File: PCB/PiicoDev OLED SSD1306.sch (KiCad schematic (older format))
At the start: 30 parts, among them J1 , J2 , J3 Conn_PiicoDev_header_01x04_Ma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, J4 Conn_01x01_Male, U2 Display_Graphic_OLED_SSD1306_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

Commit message: Update Schematic & PCB
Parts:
- added JP3: SolderJumper_2_Open, Jumper:SolderJumper-2_P1.3mm_Open_RoundedPad1.0x1.5mm, symbol Jumper:SolderJumper_2_Open
- added R6: 4k7, Resistor_SMD:R_0402_1005Metric, symbol Device:R
- C1: value 1.0u -> 2.2u; footprint Capacitor_SMD:C_0603_1608Metric -> Capacitor_SMD:C_0402_1005Metric
- C2, C3, C6, C7: footprint Capacitor_SMD:C_0603_1608Metric -> Capacitor_SMD:C_0402_1005Metric
- C4: value 100n -> 2.2u; footprint Capacitor_SMD:C_0603_1608Metric -> Capacitor_SMD:C_0402_1005Metric
- C5: value 10u -> 2.2u; footprint Capacitor_SMD:C_0603_1608Metric -> Capacitor_SMD:C_0402_1005Metric
- R1: value 1k -> 4k7
- R5: value 1K -> 4k7
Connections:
- net +3V3: now also JP3.1 (A)
- net GND: now also R6.2
- net SA0: now also JP3.2 (B), R6.1
- no-connect marks 6 -> 5
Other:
- note removed: "ToDo, check capacitor values against other designs"
- moved on the sheet: R4
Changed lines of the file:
@@
 encoding utf-8
 Sheet 1 1
-Title ""
-Date ""
-Rev ""
+Title "PiicoDev OLED SSD1306"
+Date "2021-07-09"
+Rev "00"
 Comp "Core Electronics"
-Comment1 ""
-Comment2 ""
-Comment3 ""
+Comment1 "Designed at Core Electronics by Peter Johnston"
+Comment2 "PiicoDev and the PiicoDev logo are trademarks of Core Electronics Pty Ltd"
+Comment3 "License: CCASAv4.0 http://creativecommons.org/licenses/by-sa/4.0"
 Comment4 ""
 $EndDescr
@@
 P 1450 3950
 F 0 "R1" H 1520 3996 50  0000 L CNN
-F 1 "1k" H 1520 3905 50  0000 L CNN
+F 1 "4k7" H 1520 3905 50  0000 L CNN
 F 2 "Resistor_SMD:R_0402_1005Metric" V 1380 3950 50  0001 C CNN
 F 3 "~" H 1450 3950 50  0001 C CNN
@@
 P 5400 5150
 F 0 "C1" H 5515 5196 50  0000 L CNN
-F 1 "1.0u" H 5515 5105 50  0000 L CNN
-F 2 "Capacitor_SMD:C_0603_1608Metric" H 5438 5000 50  0001 C CNN
+F 1 "2.2u" H 5515 5105 50  0000 L CNN
+F 2 "Capacitor_SMD:C_0402_1005Metric" H 5438 5000 50  0001 C CNN
 F 3 "~" H 5400 5150 50  0001 C CNN
 	1    5400 5150
@@
 F 0 "C2" H 9815 2096 50  0000 L CNN
 F 1 "2.2u" H 9815 2005 50  0000 L CNN
-F 2 "Capacitor_SMD:C_0603_1608Metric" H 9738 1900 50  0001 C CNN
+F 2 "Capacitor_SMD:C_0402_1005Metric" H 9738 1900 50  0001 C CNN
 F 3 "~" H 9700 2050 50  0001 C CNN
 	1    9700 2050
-	1    0    0    -1
-$EndComp
-$Comp
-L Device:C C4
-U 1 1 60E2EDE0
-P 5850 5150
-F 0 "C4" H 5965 5196 50  0000 L CNN
-F 1 "100n" H 5965 5105 50  0000 L CNN
-F 2 "Capacitor_SMD:C_0603_1608Metric" H 5888 5000 50  0001 C CNN
-F 3 "~" H 5850 5150 50  0001 C CNN
-	1    5850 5150
 	1    0    0    -1
 $EndComp
@@
 F 0 "C6" H 9365 2546 50  0000 L CNN
 F 1 "2.2u" H 9365 2455 50  0000 L CNN
-F 2 "Capacitor_SMD:C_0603_1608Metric" H 9288 2350 50  0001 C CNN
+F 2 "Capacitor_SMD:C_0402_1005Metric" H 9288 2350 50  0001 C CNN
 F 3 "~" H 9250 2500 50  0001 C CNN
 	1    9250 2500
@@
 L Device:R R4
 U 1 1 60E30177
-P 7500 3700
-F 0 "R4" H 7570 3746 50  0000 L CNN
-F 1 "390K" H 7570 3655 50  0000 L CNN
-F 2 "Resistor_SMD:R_0402_1005Metric" V 7430 3700 50  0001 C CNN
-F 3 "~" H 7500 3700 50  0001 C CNN
-	1    7500 3700
+P 7400 3700
+F 0 "R4" H 7470 3746 50  0000 L CNN
+F 1 "390K" H 7470 3655 50  0000 L CNN
+F 2 "Resistor_SMD:R_0402_1005Metric" V 7330 3700 50  0001 C CNN
+F 3 "~" H 7400 3700 50  0001 C CNN
+	1    7400 3700
 	1    0    0    -1
 $EndComp
@@
 F 0 "C3" H 9365 3746 50  0000 L CNN
 F 1 "2.2u" H 9365 3655 50  0000 L CNN
-F 2 "Capacitor_SMD:C_0603_1608Metric" H 9288 3550 50  0001 C CNN
+F 2 "Capacitor_SMD:C_0402_1005Metric" H 9288 3550 50  0001 C CNN
 F 3 "~" H 9250 3700 50  0001 C CNN
 	1    9250 3700
@@
 F 0 "C7" H 9365 3146 50  0000 L CNN
 F 1 "2.2u" H 9365 3055 50  0000 L CNN
-F 2 "Capacitor_SMD:C_0603_1608Metric" H 9288 2950 50  0001 C CNN
+F 2 "Capacitor_SMD:C_0402_1005Metric" H 9288 2950 50  0001 C CNN
 F 3 "~" H 9250 3100 50  0001 C CNN
 	1    9250 3100
@@
 $EndComp
 Wire Wire Line
-	6300 2600 6300 2700
-Wire Wire Line
 	6300 3500 6300 3600
 $Comp
@@
 	1    0    0    -1
 $EndComp
-Wire Wire Line
-	7950 3200 7700 3200
 Text Label 7700 3200 0    50   ~ 0
 SA0
@@
 Wire Wire Line
 	2950 2000 3150 2000
-Wire Wire Line
-	7500 5150 8400 5150
 Connection ~ 8400 5150
-Wire Wire Line
-	7500 3850 7500 5150
-Wire Wire Line
-	7400 3400 7400 5150
-Wire Wire Line
-	7400 5150 7500 5150
-Wire Wire Line
-	7400 3400 7950 3400
-Connection ~ 7500 5150
-Wire Wire Line
-	7400 3300 7400 3400
-Wire Wire Line
-	7400 3300 7950 3300
-Connection ~ 7400 3400
-Wire Wire Line
-	7950 3500 7500 3500
-Wire Wire Line
-	7500 3500 7500 3550
-Wire Wire Line
-	5400 5000 5400 4950
-Wire Wire Line
-	5400 4950 5850 4950
-Wire Wire Line
-	5850 4950 5850 5000
-Wire Wire Line
-	5400 5300 5400 5350
-Wire Wire Line
-	5400 5350 5850 5350
-Wire Wire Line
-	5850 5350 5850 5300
 $Comp
 L power:GND #PWR02
@@
 $EndComp
 Wire Wire Line
-	5400 4900 5400 4950
-Connection ~ 5400 4950
-Wire Wire Line
-	5400 5350 5400 5400
-Connection ~ 5400 5350
-Wire Wire Line
 	7950 2700 7500 2700
 Connection ~ 7500 2700
 Wire Wire Line
 	7500 2700 7500 1850
-Wire Wire Line
-	7950 2800 7400 2800
-Wire Wire Line
-	7400 2800 7400 3300
-Connection ~ 7400 3300
-Wire Wire Line
-	7950 2600 7400 2600
-Wire Wire Line
-	7400 2600 7400 2800
-Connection ~ 7400 2800
-Text Notes 4600 1750 0    50   ~ 0
-ToDo, check capacitor values against other designs
 $Comp
 L CoreElectronics_Components:Display_Graphic_OLED_SSD1306_30-Pin U2
@@
 NoConn ~ 7950 4300
 NoConn ~ 7950 4400
-NoConn ~ 2650 4150
 $Comp
 L Device:R R5
@@
 P 6300 2850
 F 0 "R5" H 6370 2896 50  0000 L CNN
-F 1 "1K" H 6370 2805 50  0000 L CNN
+F 1 "4k7" H 6370 2805 50  0000 L CNN
 F 2 "Resistor_SMD:R_0402_1005Metric" V 6230 2850 50  0001 C CNN
 F 3 "~" H 6300 2850 50  0001 C CNN
@@
 P 6300 3350
 F 0 "C5" H 6415 3396 50  0000 L CNN
-F 1 "10u" H 6415 3305 50  0000 L CNN
-F 2 "Capacitor_SMD:C_0603_1608Metric" H 6338 3200 50  0001 C CNN
+F 1 "2.2u" H 6415 3305 50  0000 L CNN
+F 2 "Capacitor_SMD:C_0402_1005Metric" H 6338 3200 50  0001 C CNN
 F 3 "~" H 6300 3350 50  0001 C CNN
 	1    6300 3350
@@
 Wire Wire Line
 	6300 3000 6300 3100
-Wire Wire Line
-	6300 3100 7950 3100
 Connection ~ 6300 3100
 Wire Wire Line
@@
 	1    0    0    -1
 $EndComp
+$Comp
+L Jumper:SolderJumper_2_Open JP3
+U 1 1 60E6C696
+P 6750 2900
+F 0 "JP3" V 6704 2968 50  0000 L CNN
+F 1 "SolderJumper_2_Open" V 6795 2968 50  0000 L CNN
+F 2 "Jumper:SolderJumper-2_P1.3mm_Open_RoundedPad1.0x1.5mm" H 6750 2900 50  0001 C CNN
+F 3 "~" H 6750 2900 50  0001 C CNN
+	1    6750 2900
+	0    1    1    0
+$EndComp
+$Comp
+L Device:R R6
+U 1 1 60E73C8C
+P 6750 3400
+F 0 "R6" H 6820 3446 50  0000 L CNN
+F 1 "4k7" H 6820 3355 50  0000 L CNN
+F 2 "Resistor_SMD:R_0402_1005Metric" V 6680 3400 50  0001 C CNN
+F 3 "~" H 6750 3400 50  0001 C CNN
+	1    6750 3400
+	1    0    0    -1
+$EndComp
+Wire Wire Line
+	6300 2600 6300 2700
+Connection ~ 7500 1850
+Wire Wire Line
+	6750 3200 6750 3050
+Wire Wire Line
+	6750 3200 6750 3250
+Connection ~ 6750 3200
+Wire Wire Line
+	6750 2750 6750 1850
+Wire Wire Line
+	6750 3550 6750 5150
+Wire Wire Line
+	6750 1850 7500 1850
+Wire Wire Line
+	6750 5150 7200 5150
+Wire Wire Line
+	6300 3100 7950 3100
+Wire Wire Line
+	6750 3200 7950 3200
+Wire Wire Line
+	7200 2600 7200 2800
+Connection ~ 7200 5150
+Connection ~ 7200 3400
+Wire Wire Line
+	7200 3400 7200 5150
+Connection ~ 7200 3300
+Wire Wire Line
+	7200 3300 7200 3400
+Connection ~ 7200 2800
+Wire Wire Line
+	7200 2800 7200 3300
+Wire Wire Line
+	7200 2800 7950 2800
+Wire Wire Line
+	7200 3300 7950 3300
+Wire Wire Line
+	7200 2600 7950 2600
+Wire Wire Line
+	7200 3400 7950 3400
+Wire Wire Line
+	7400 3500 7400 3550
+Wire Wire Line
+	7400 3850 7400 5150
+Wire Wire Line
+	7200 5150 7400 5150
+Connection ~ 7400 5150
+Wire Wire Line
+	7400 5150 8400 5150
+Wire Wire Line
+	7400 3500 7950 3500
+Wire Wire Line
+	5400 4900 5400 4950
+Wire Wire Line
+	5400 5300 5400 5350
+$Comp
+L Device:C C4
+U 1 1 60E815F0
+P 5900 5150
+F 0 "C4" H 6015 5196 50  0000 L CNN
+F 1 "2.2u" H 6015 5105 50  0000 L CNN
+F 2 "Capacitor_SMD:C_0402_1005Metric" H 5938 5000 50  0001 C CNN
+F 3 "~" H 5900 5150 50  0001 C CNN
+	1    5900 5150
+	1    0    0    -1
+$EndComp
+Wire Wire Line
+	5900 5300 5900 5350
+Wire Wire Line
+	5400 4950 5900 4950
+Connection ~ 5400 4950
+Wire Wire Line
+	5400 4950 5400 5000
+Wire Wire Line
+	5900 4950 5900 5000
+Wire Wire Line
+	5400 5350 5900 5350
+Connection ~ 5400 5350
+Wire Wire Line
+	5400 5350 5400 5400
 $EndSCHEMATC

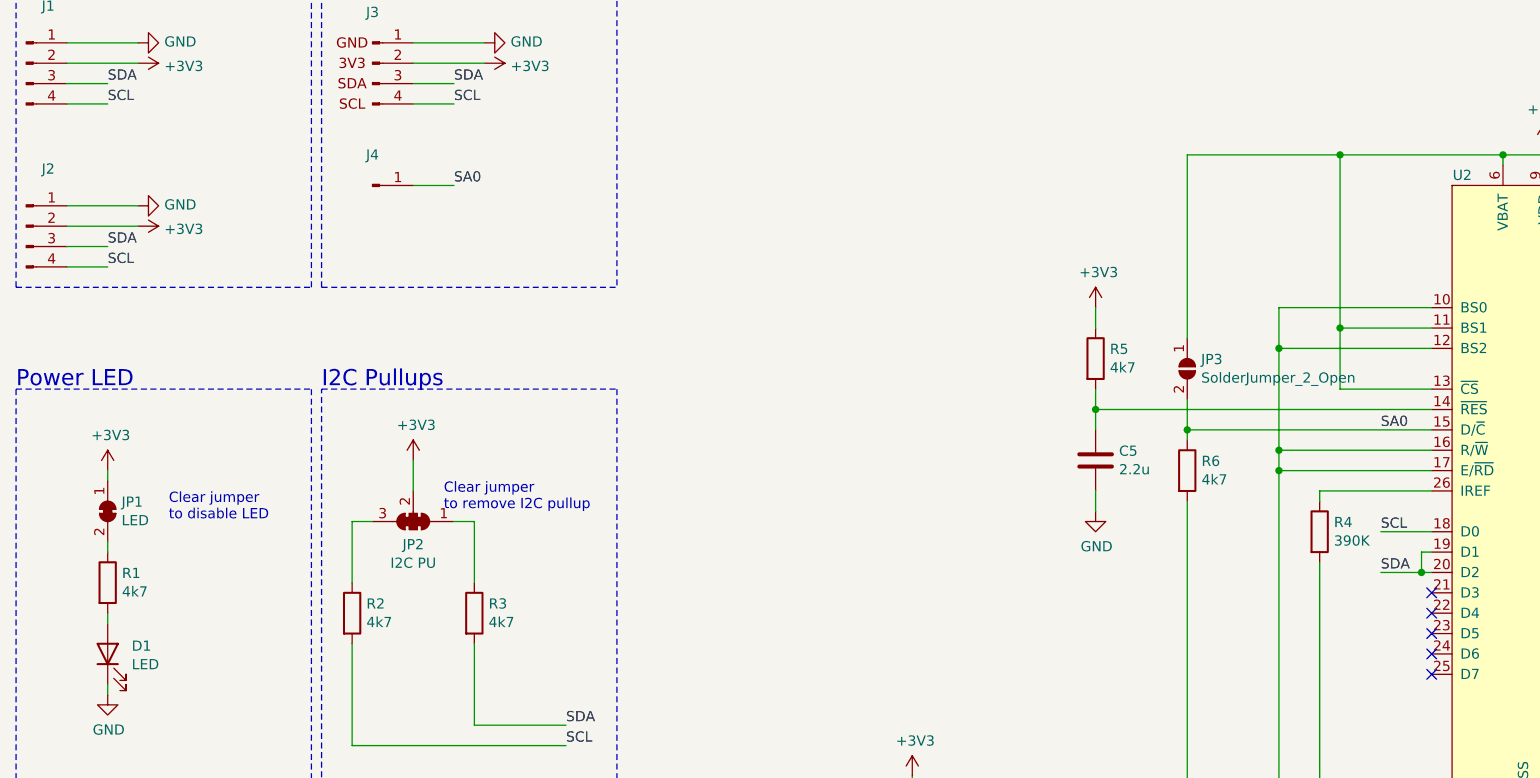
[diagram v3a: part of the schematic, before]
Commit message: v11 Update
Change resistor values
Add DIP switch and remove ADR jumper
Update graphic labels
Update text formatting
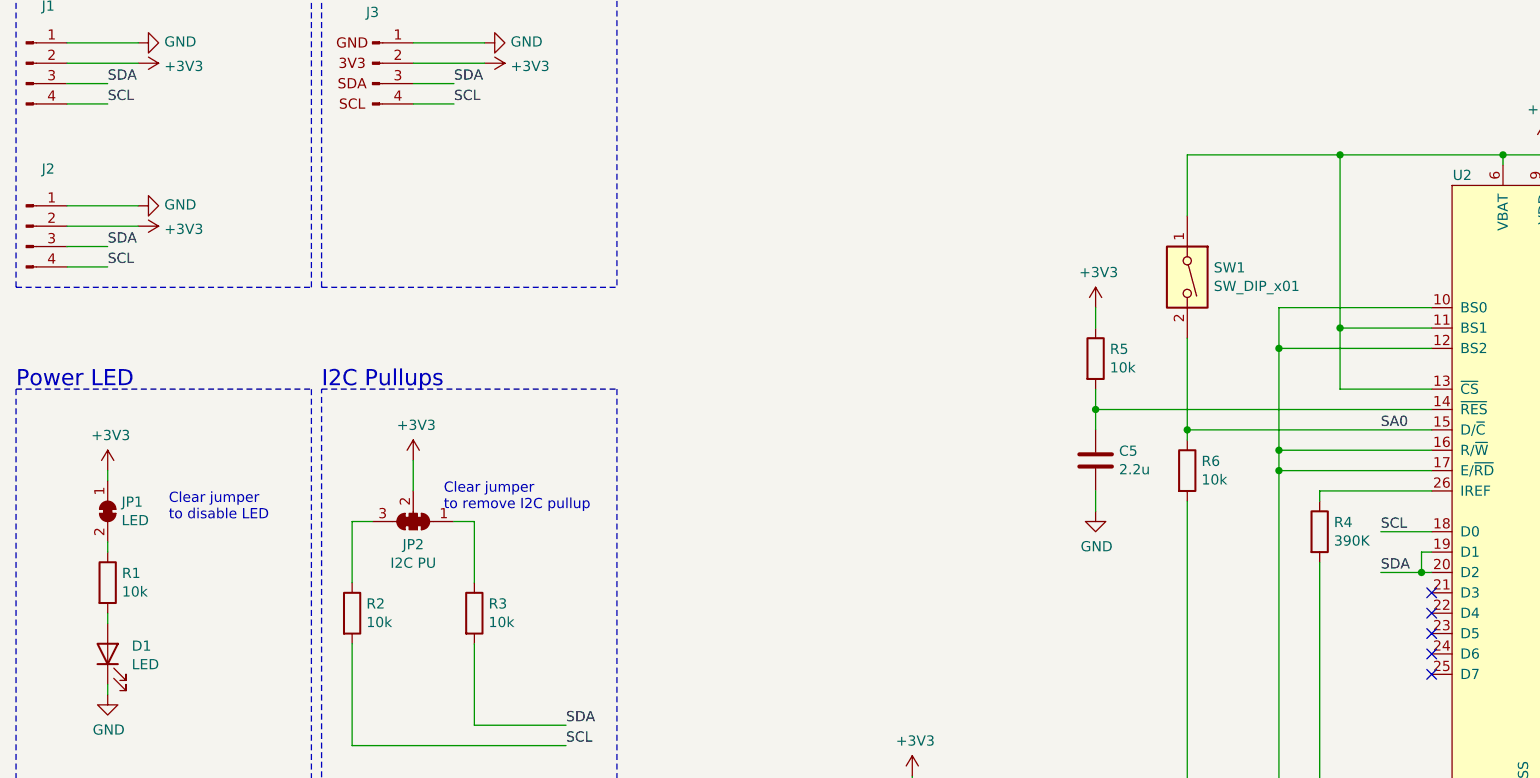
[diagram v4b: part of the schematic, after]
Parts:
- removed G1: LOGO_PiicoDev, CoreElectronics_Artwork:piicodev_logo_14.2x3.4mm, symbol CoreElectronics_Artwork:LOGO_PiicoDev
- removed J4: Conn_01x01_Male, CoreElectronics_Components:PiicoDev_header_1pin_ADR, symbol Connector:Conn_01x01_Male
- removed JP3: SolderJumper_2_Open, Jumper:SolderJumper-2_P1.3mm_Open_RoundedPad1.0x1.5mm, symbol Jumper:SolderJumper_2_Open
- added SW1: SW_DIP_x01, CoreElectronics_Components:SW_DIP_x01_Slide_CHS-01A1, symbol Switch:SW_DIP_x01
- J3: footprint CoreElectronics_Components:PiicoDev_header_4pin -> CoreElectronics_Components:PiicoDev_header_4pin_no_labels
- R1, R2, R3, R5, R6: value 4k7 -> 10k
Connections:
- net +3V3: now also SW1.1
- net SA0: now also SW1.2
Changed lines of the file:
@@
 Sheet 1 1
 Title "PiicoDev OLED SSD1306"
-Date "2021-08-20"
-Rev "10"
+Date "2021-12-30"
+Rev "11"
 Comp "Core Electronics"
 Comment1 "Designed at Core Electronics by Peter Johnston"
@@
 $EndDescr
 $Comp
-L CoreElectronics_Artwork:LOGO_PiicoDev G1
+L CoreElectronics_Artwork:LOGO_PiicoDev #G1
 U 1 1 609A2A66
 P 8000 6300
-F 0 "G1" H 8000 6076 60  0001 C CNN
+F 0 "#G1" H 8000 6076 60  0001 C CNN
 F 1 "LOGO_PiicoDev" H 8000 6590 60  0001 C CNN
-F 2 "CoreElectronics_Artwork:piicodev_logo_14.2x3.4mm" H 8000 6300 50  0001 C CNN
+F 2 "" H 8000 6300 50  0001 C CNN
 F 3 "" H 8000 6300 50  0001 C CNN
 	1    8000 6300
@@
 F 0 "J3" H 2750 1850 50  0000 C CNN
 F 1 "Conn_PiicoDev_header_01x04_Male" H 2771 1807 50  0001 C CNN
-F 2 "CoreElectronics_Components:PiicoDev_header_4pin" H 2750 1500 50  0001 C CNN
+F 2 "CoreElectronics_Components:PiicoDev_header_4pin_no_labels" H 2750 1500 50  0001 C CNN
 F 3 "~" H 2750 1500 50  0001 C CNN
 	1    2750 1500
@@
 AR Path="/60A08162" Ref="R3"  Part="1"
 F 0 "R3" H 3320 4146 50  0000 L CNN
-F 1 "4k7" H 3320 4055 50  0000 L CNN
+F 1 "10k" H 3320 4055 50  0000 L CNN
 F 2 "Resistor_SMD:R_0402_1005Metric" V 3180 4100 50  0001 C CNN
 F 3 "~" H 3250 4100 50  0001 C CNN
@@
 AR Path="/60A08170" Ref="R2"  Part="1"
 F 0 "R2" H 2720 4146 50  0000 L CNN
-F 1 "4k7" H 2720 4055 50  0000 L CNN
+F 1 "10k" H 2720 4055 50  0000 L CNN
 F 2 "Resistor_SMD:R_0402_1005Metric" V 2580 4100 50  0001 C CNN
 F 3 "~" H 2650 4100 50  0001 C CNN
@@
 P 1450 3950
 F 0 "R1" H 1520 3996 50  0000 L CNN
-F 1 "4k7" H 1520 3905 50  0000 L CNN
+F 1 "10k" H 1520 3905 50  0000 L CNN
 F 2 "Resistor_SMD:R_0402_1005Metric" V 1380 3950 50  0001 C CNN
 F 3 "~" H 1450 3950 50  0001 C CNN
@@
 Text Label 7700 3200 0    50   ~ 0
 SA0
-Text Label 3150 2000 0    50   ~ 0
-SA0
-$Comp
-L Connector:Conn_01x01_Male J4
-U 1 1 60E7BAB8
-P 2750 2000
-F 0 "J4" H 2750 2150 50  0000 C CNN
-F 1 "Conn_01x01_Male" H 2858 2090 50  0001 C CNN
-F 2 "CoreElectronics_Components:PiicoDev_header_1pin_ADR" H 2750 2000 50  0001 C CNN
-F 3 "~" H 2750 2000 50  0001 C CNN
-	1    2750 2000
-	1    0    0    -1
-$EndComp
-Wire Wire Line
-	2950 2000 3150 2000
 Connection ~ 8400 5150
 $Comp
@@
 P 6300 2850
 F 0 "R5" H 6370 2896 50  0000 L CNN
-F 1 "4k7" H 6370 2805 50  0000 L CNN
+F 1 "10k" H 6370 2805 50  0000 L CNN
 F 2 "Resistor_SMD:R_0402_1005Metric" V 6230 2850 50  0001 C CNN
 F 3 "~" H 6300 2850 50  0001 C CNN
@@
 $EndComp
 $Comp
-L Jumper:SolderJumper_2_Open JP3
-U 1 1 60E6C696
-P 6750 2900
-F 0 "JP3" V 6704 2968 50  0000 L CNN
-F 1 "SolderJumper_2_Open" V 6795 2968 50  0000 L CNN
-F 2 "Jumper:SolderJumper-2_P1.3mm_Open_RoundedPad1.0x1.5mm" H 6750 2900 50  0001 C CNN
-F 3 "~" H 6750 2900 50  0001 C CNN
-	1    6750 2900
-	0    1    1    0
-$EndComp
-$Comp
 L Device:R R6
 U 1 1 60E73C8C
 P 6750 3400
 F 0 "R6" H 6820 3446 50  0000 L CNN
-F 1 "4k7" H 6820 3355 50  0000 L CNN
+F 1 "10k" H 6820 3355 50  0000 L CNN
 F 2 "Resistor_SMD:R_0402_1005Metric" V 6680 3400 50  0001 C CNN
 F 3 "~" H 6750 3400 50  0001 C CNN
@@
 Connection ~ 7500 1850
 Wire Wire Line
-	6750 3200 6750 3050
-Wire Wire Line
 	6750 3200 6750 3250
 Connection ~ 6750 3200
-Wire Wire Line
-	6750 2750 6750 1850
 Wire Wire Line
 	6750 3550 6750 5150
@@
 Wire Wire Line
 	5400 5350 5400 5400
+$Comp
+L Switch:SW_DIP_x01 SW1
+U 1 1 61CD3BB7
+P 6750 2450
+F 0 "SW1" V 6704 2580 50  0000 L CNN
+F 1 "SW_DIP_x01" V 6795 2580 50  0000 L CNN
+F 2 "CoreElectronics_Components:SW_DIP_x01_Slide_CHS-01A1" H 6750 2450 50  0001 C CNN
+F 3 "~" H 6750 2450 50  0001 C CNN
+	1    6750 2450
+	0    1    1    0
+$EndComp
+Wire Wire Line
+	6750 2750 6750 3200
+Wire Wire Line
+	6750 2150 6750 1850
 $EndSCHEMATC
